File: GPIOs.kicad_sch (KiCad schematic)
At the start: 0 parts

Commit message: [feat] Add CAN transceiver SN65VHD230
Also ran ERC checks and add some exclusion ERC for the FT230XS due to
3V3OUT being an input pin rather than output pin
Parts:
- added J2: SWD, symbol Connector:Conn_01x03_Pin
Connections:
- new net SWCLK: J2.2 (Pin_2)
- new net SWDIO: J2.1 (Pin_1)
- new net TRACE_SWO: J2.3 (Pin_3)
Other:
- note added: "Serial Wire Debugger"
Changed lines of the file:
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@@
 	(generator_version "10.0")
 	(paper "A4")
+	(rectangle
+		(start 19.05 20.32)
+		(end 55.88 39.37)
+		(stroke
+			(width 0)
+			(type default)
+		)
+		(fill
+			(type none)
+		)
+	)
+	(text "Serial Wire Debugger"
+		(exclude_from_sim no)
+		(at 28.702 18.542 0)
+		(effects
+			(font
+				(size 1.27 1.27)
+			)
+		)
+	)
+	(wire
+		(pts
+			(xy 30.48 29.21) (xy 35.56 29.21)
+		)
+		(stroke
+			(width 0)
+			(type default)
+		)
+	)
+	(wire
+		(pts
+			(xy 30.48 31.75) (xy 35.56 31.75)
+		)
+		(stroke
+			(width 0)
+			(type default)
+		)
+	)
+	(wire
+		(pts
+			(xy 30.48 34.29) (xy 35.56 34.29)
+		)
+		(stroke
+			(width 0)
+			(type default)
+		)
+	)
+	(hierarchical_label "SWDIO"
+		(shape input)
+		(at 35.56 29.21 0)
+		(effects
+			(font
+				(size 1.27 1.27)
+			)
+			(justify left)
+		)
+	)
+	(hierarchical_label "TRACE_SWO"
+		(shape input)
+		(at 35.56 34.29 0)
+		(effects
+			(font
+				(size 1.27 1.27)
+			)
+			(justify left)
+		)
+	)
+	(hierarchical_label "SWCLK"
+		(shape input)
+		(at 35.56 31.75 0)
+		(effects
+			(font
+				(size 1.27 1.27)
+			)
+			(justify left)
+		)
+	)
+	(symbol
+		(lib_id "Connector:Conn_01x03_Pin")
+		(at 25.4 31.75 0)
+		(unit 1)
+		(body_style 1)
+		(exclude_from_sim no)
+		(in_bom yes)
+		(on_board yes)
+		(in_pos_files yes)
+		(dnp no)
+		(fields_autoplaced yes)
+		(property "Reference" "J2"
+			(at 26.035 24.13 0)
+			(show_name no)
+			(do_not_autoplace no)
+			(effects
+				(font
+					(size 1.27 1.27)
+				)
+			)
+		)
+		(property "Value" "SWD"
+			(at 26.035 26.67 0)
+			(show_name no)
+			(do_not_autoplace no)
+			(effects
+				(font
+					(size 1.27 1.27)
+				)
+			)
+		)
+		(property "Footprint" ""
+			(at 25.4 31.75 0)
+			(hide yes)
+			(show_name no)
+			(do_not_autoplace no)
+			(effects
+				(font
+					(size 1.27 1.27)
+				)
+			)
+		)
+		(property "Datasheet" ""
+			(at 25.4 31.75 0)
+			(hide yes)
+			(show_name no)
+			(do_not_autoplace no)
+			(effects
+				(font
+					(size 1.27 1.27)
+				)
+			)
+		)
+		(property "Description" "Generic connector, single row, 01x03, script generated"
+			(at 25.4 31.75 0)
+			(hide yes)
+			(show_name no)
+			(do_not_autoplace no)
+			(effects
+				(font
+					(size 1.27 1.27)
+				)
+			)
+		)
+		(pin "1"
+		)
+		(pin "2"
+		)
+		(pin "3"
+		)
+		(instances
+			(project "owl_v1"
+				(path "/c1d8d3e2-84ea-437a-bbb1-a2e651deb7ac/d52cdafd-bcb4-4a55-a779-8e3cd50df227"
+					(reference "J2")
+					(unit 1)
+				)
+			)
+		)
+	)
 )

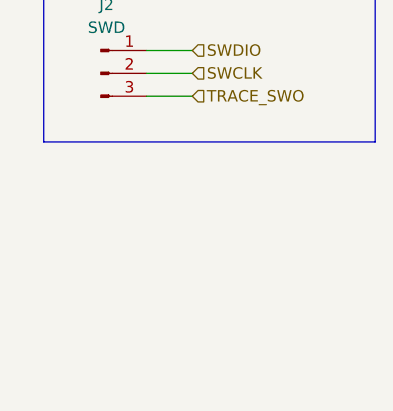
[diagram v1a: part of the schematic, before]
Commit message: [feat] Add breakout for SPI1 for IMU
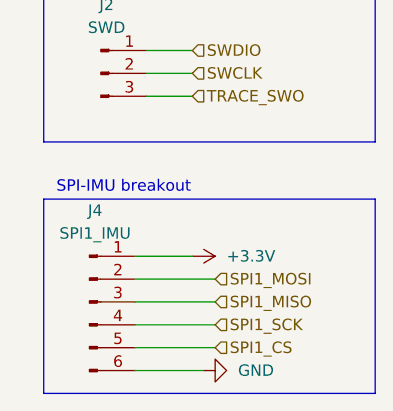
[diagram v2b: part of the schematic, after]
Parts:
- added J4: SPI1_IMU, Connector_PinHeader_2.54mm:PinHeader_1x06_P2.54mm_Vertical, symbol Connector:Conn_01x06_Pin
- J2: footprint (none) -> Connector_PinHeader_2.54mm:PinHeader_1x03_P2.54mm_Vertical; now left out of the parts list
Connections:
- new net +3.3V: J4.1 (Pin_1)
- new net GND: J4.6 (Pin_6)
- new net SPI1_CS: J4.5 (Pin_5)
- new net SPI1_MISO: J4.3 (Pin_3)
- new net SPI1_MOSI: J4.2 (Pin_2)
- new net SPI1_SCK: J4.4 (Pin_4)
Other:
- note added: "SPI-IMU breakout"

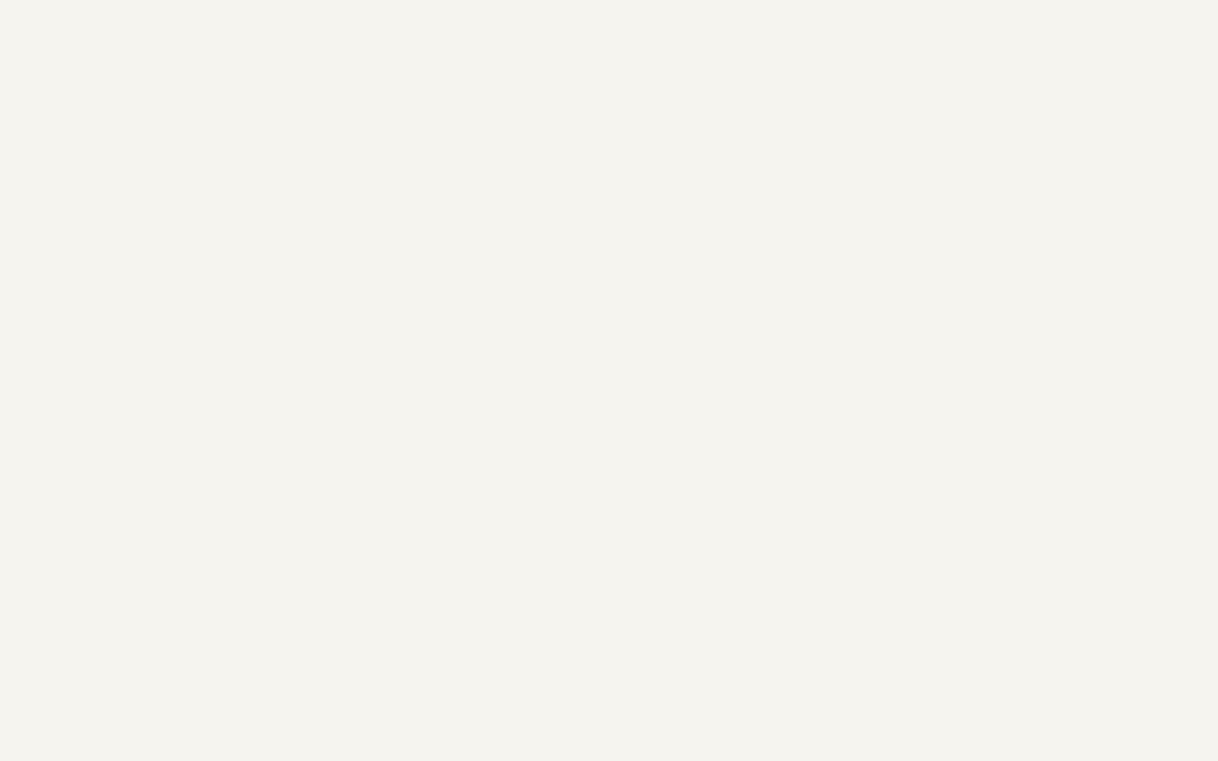
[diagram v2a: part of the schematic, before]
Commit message: [feat] Integrate MicroSD Card into the board with SPI2
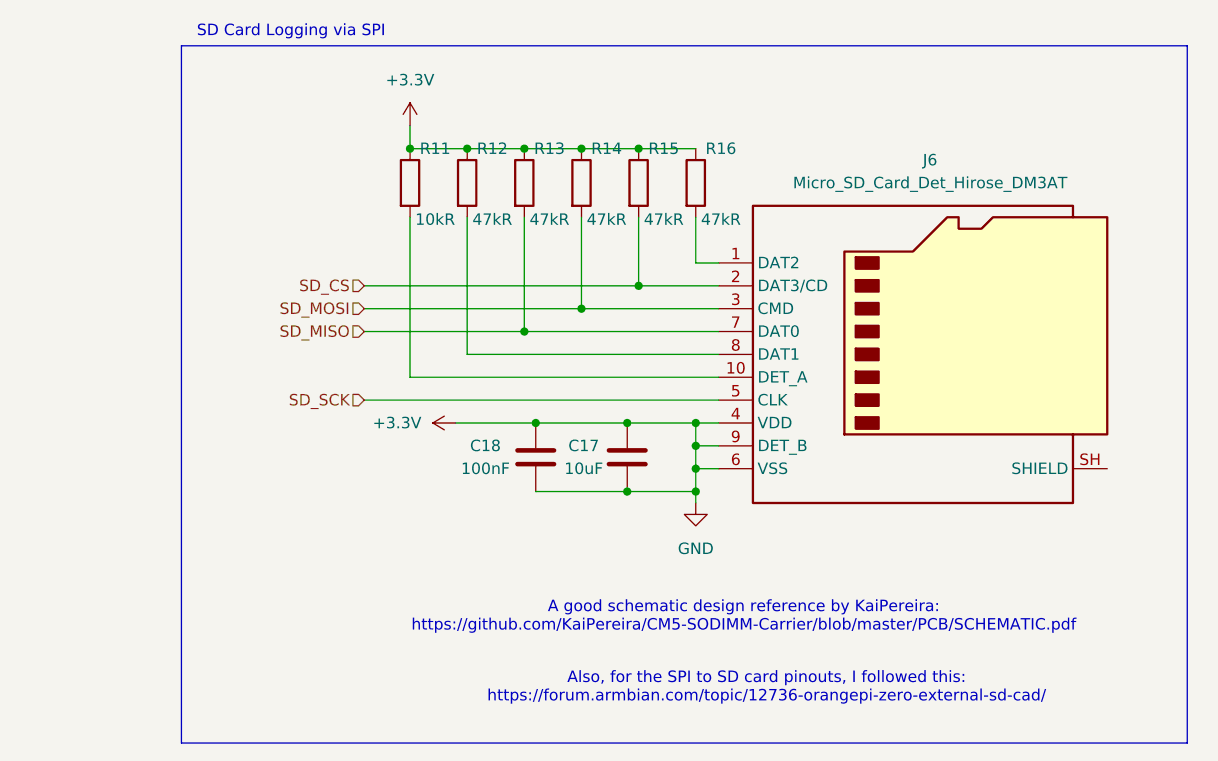
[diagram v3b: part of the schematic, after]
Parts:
- added C17: 10uF, Capacitor_SMD:C_0603_1608Metric, symbol Device:C
- added C18: 100nF, Capacitor_SMD:C_0603_1608Metric, symbol Device:C
- added J6: Micro_SD_Card_Det_Hirose_DM3AT, Connector_Card:microSD_HC_Hirose_DM3AT-SF-PEJM5, symbol Connector:Micro_SD_Card_Det_Hirose_DM3AT
- added R11: 10kR, Resistor_SMD:R_0603_1608Metric, symbol Device:R
- added R12, R13, R14, R15, R16: 47kR, Resistor_SMD:R_0603_1608Metric, symbol Device:R
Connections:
- net GND is gone; now on net +3.3V: J4.6 (Pin_6)
- net +3.3V: now also C17.1, C17.2, C18.1, C18.2, J6.4 (VDD), J6.6 (VSS), J6.9 (DET_B), R11.1, R12.1, R13.1, R14.1, R15.1, R16.1
- new net: J6.1 (DAT2), R16.2
- new net: J6.10 (DET_A), R11.2
- new net: J6.8 (DAT1), R12.2
- new net SD_CS: J6.2 (DAT3/CD), R15.2
- new net SD_MISO: J6.7 (DAT0), R13.2
- new net SD_MOSI: J6.3 (CMD), R14.2
- new net SD_SCK: J6.5 (CLK)
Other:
- note added: "A good schematic design reference by KaiPereira: https://github.com/KaiPereira/CM5-SODIMM-Carrier/blob/master/PCB/SCHEMATIC.pdf"
- note added: "Also, for the SPI to SD card pinouts, I followed this: https://forum.armbian.com/topic/12736-orangepi-zero-external-sd-cad/"
- note added: "SD Card Logging via SPI"

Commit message: [feat] Add I2C breakout
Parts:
- added J5: I2C, Connector_PinHeader_2.54mm:PinHeader_1x04_P2.54mm_Vertical, symbol Connector:Conn_01x04_Pin
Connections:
- net +3.3V: now also J5.1 (Pin_1), J5.4 (Pin_4)
- new net I2C_SCLK: J5.3 (Pin_3)
- new net I2C_SDA: J5.2 (Pin_2)
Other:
- note added: "I2C Breakout"
- note added: "I2C_CS can be used via GPIO"
- moved on the sheet: C17, C18, J6, R11, R12, R13, R14, R15, R16

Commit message: [feat] Add OLED I2C breakout for display, Add general purpose GPIOs
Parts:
- added J7: I2C OLED, Connector_PinSocket_2.54mm:PinSocket_1x04_P2.54mm_Vertical, symbol Connector:Conn_01x04_Socket
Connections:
- net +3.3V: now also J7.1 (Pin_1); no longer C17.2, C18.2, J4.6 (Pin_6), J5.4 (Pin_4), J6.6 (VSS), J6.9 (DET_B)
- new net GND: C17.2, C18.2, J4.6 (Pin_6), J5.4 (Pin_4), J6.6 (VSS), J6.9 (DET_B), J7.2 (Pin_2)
- new net OLED_SCL: J7.3 (Pin_3)
- new net OLED_SDA: J7.4 (Pin_4)
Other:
- note added: "0.96" OLED Display Module (128x64)"
- note added: "I2C Display to use"
- note added: "OLED Display Module Integration"

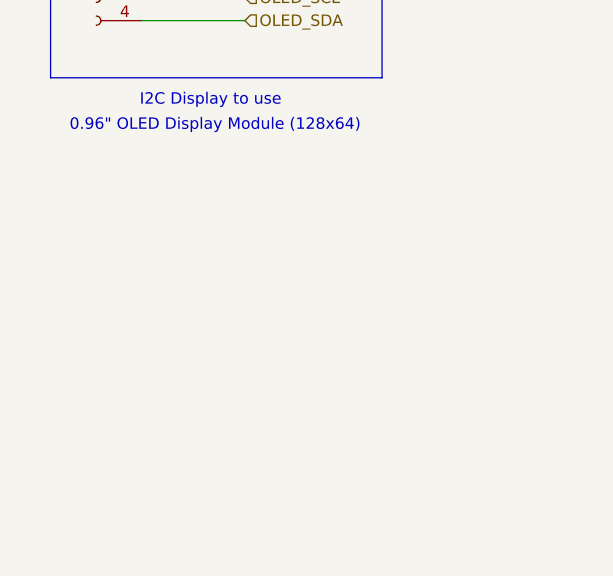
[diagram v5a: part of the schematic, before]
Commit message: [feat] Add footprints for external GPIOs
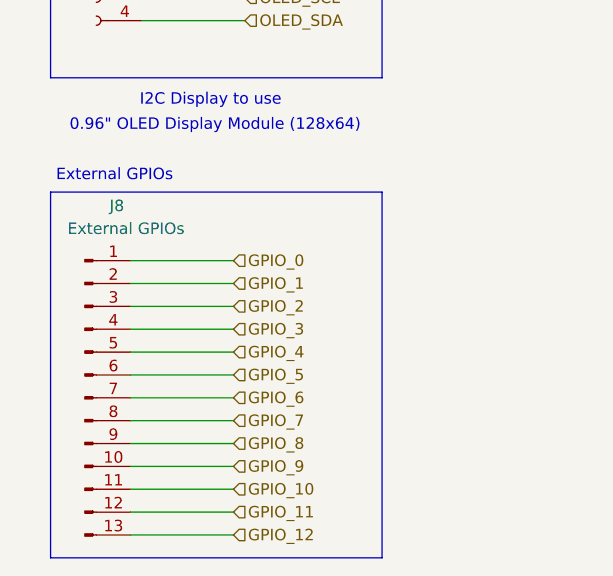
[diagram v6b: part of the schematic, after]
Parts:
- added J8: External GPIOs, Connector_PinHeader_2.54mm:PinHeader_1x13_P2.54mm_Vertical, symbol Connector:Conn_01x13_Pin
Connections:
- new net GPIO_0: J8.1 (Pin_1)
- new net GPIO_1: J8.2 (Pin_2)
- new net GPIO_10: J8.11 (Pin_11)
- new net GPIO_11: J8.12 (Pin_12)
- new net GPIO_12: J8.13 (Pin_13)
- new net GPIO_2: J8.3 (Pin_3)
- new net GPIO_3: J8.4 (Pin_4)
- new net GPIO_4: J8.5 (Pin_5)
- new net GPIO_5: J8.6 (Pin_6)
- new net GPIO_6: J8.7 (Pin_7)
- new net GPIO_7: J8.8 (Pin_8)
- new net GPIO_8: J8.9 (Pin_9)
- new net GPIO_9: J8.10 (Pin_10)
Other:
- note added: "External GPIOs"

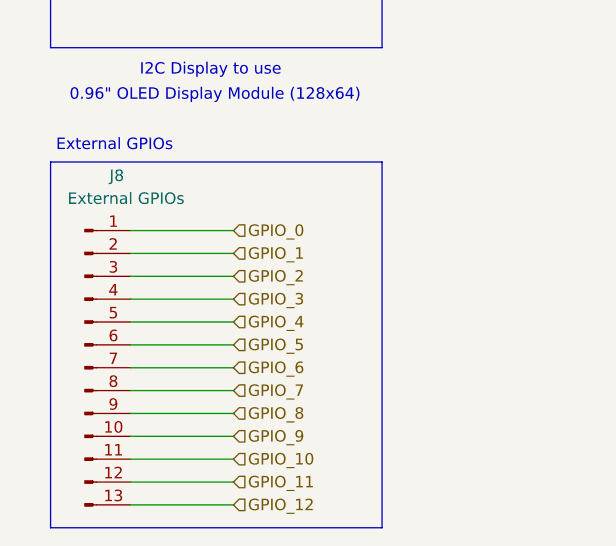
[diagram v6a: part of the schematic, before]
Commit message: [refactor] Remove GPIO12 and GPIO13 for LED green and blue
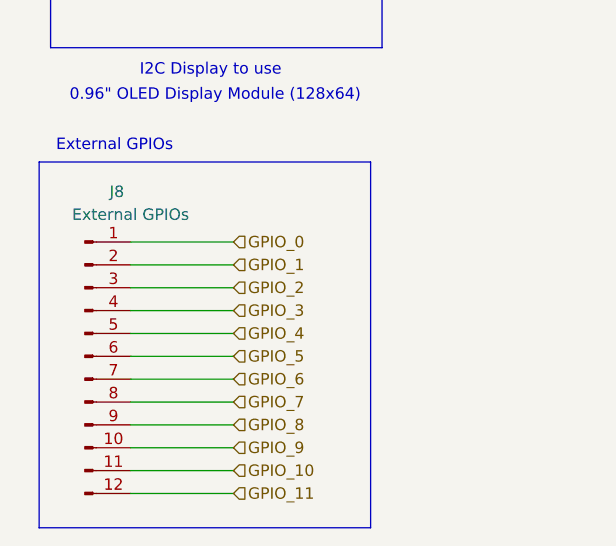
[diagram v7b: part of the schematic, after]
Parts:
- J8: symbol Connector:Conn_01x13_Pin -> Connector:Conn_01x12_Pin
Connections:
- removed net GPIO_12: J8.13 (Pin_13)
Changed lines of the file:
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@@
 	(paper "A4")
 	(rectangle
-		(start 19.05 142.24)
-		(end 55.88 182.88)
+		(start 17.78 142.24)
+		(end 54.61 182.88)
 		(stroke
 			(width 0)
@@
 	(wire
 		(pts
-			(xy 27.94 152.4) (xy 39.37 152.4)
+			(xy 27.94 171.45) (xy 39.37 171.45)
+		)
+		(stroke
+			(width 0)
+			(type default)
+		)
+	)
+	(wire
+		(pts
+			(xy 27.94 168.91) (xy 39.37 168.91)
 		)
 		(stroke
@@
 	(wire
 		(pts
-			(xy 27.94 154.94) (xy 39.37 154.94)
-		)
-		(stroke
-			(width 0)
-			(type default)
-		)
-	)
-	(wire
-		(pts
 			(xy 121.92 44.45) (xy 124.46 44.45)
 		)
@@
 	(wire
 		(pts
-			(xy 27.94 175.26) (xy 39.37 175.26)
+			(xy 27.94 153.67) (xy 39.37 153.67)
 		)
 		(stroke
@@
 	(wire
 		(pts
-			(xy 27.94 167.64) (xy 39.37 167.64)
-		)
-		(stroke
-			(width 0)
-			(type default)
-		)
-	)
-	(wire
-		(pts
-			(xy 27.94 160.02) (xy 39.37 160.02)
-		)
-		(stroke
-			(width 0)
-			(type default)
-		)
-	)
-	(wire
-		(pts
 			(xy 29.21 118.11) (xy 39.37 118.11)
 		)
@@
 	(wire
 		(pts
+			(xy 27.94 173.99) (xy 39.37 173.99)
+		)
+		(stroke
+			(width 0)
+			(type default)
+		)
+	)
+	(wire
+		(pts
 			(xy 104.14 69.85) (xy 114.3 69.85)
 		)
@@
 	(wire
 		(pts
-			(xy 27.94 157.48) (xy 39.37 157.48)
+			(xy 27.94 179.07) (xy 39.37 179.07)
 		)
 		(stroke
@@
 	(wire
 		(pts
+			(xy 27.94 163.83) (xy 39.37 163.83)
+		)
+		(stroke
+			(width 0)
+			(type default)
+		)
+	)
+	(wire
+		(pts
 			(xy 29.21 123.19) (xy 40.64 123.19)
 		)
@@
 	(wire
 		(pts
+			(xy 27.94 166.37) (xy 39.37 166.37)
+		)
+		(stroke
+			(width 0)
+			(type default)
+		)
+	)
+	(wire
+		(pts
 			(xy 124.46 67.31) (xy 121.92 67.31)
 		)
@@
 	(wire
 		(pts
+			(xy 27.94 161.29) (xy 39.37 161.29)
+		)
+		(stroke
+			(width 0)
+			(type default)
+		)
+	)
+	(wire
+		(pts
 			(xy 29.21 64.77) (xy 36.83 64.77)
 		)
@@
 	(wire
 		(pts
-			(xy 27.94 165.1) (xy 39.37 165.1)
+			(xy 27.94 158.75) (xy 39.37 158.75)
 		)
 		(stroke
@@
 	(wire
 		(pts
-			(xy 27.94 172.72) (xy 39.37 172.72)
-		)
-		(stroke
-			(width 0)
-			(type default)
-		)
-	)
-	(wire
-		(pts
 			(xy 121.92 39.37) (xy 121.92 44.45)
 		)
@@
 	(wire
 		(pts
-			(xy 27.94 162.56) (xy 39.37 162.56)
-		)
-		(stroke
-			(width 0)
-			(type default)
-		)
-	)
-	(wire
-		(pts
 			(xy 115.57 31.75) (xy 121.92 31.75)
 		)
@@
 	(wire
 		(pts
-			(xy 27.94 170.18) (xy 39.37 170.18)
-		)
-		(stroke
-			(width 0)
-			(type default)
-		)
-	)
-	(wire
-		(pts
 			(xy 85.09 49.53) (xy 109.22 49.53)
 		)
@@
 	(wire
 		(pts
-			(xy 27.94 180.34) (xy 39.37 180.34)
-		)
-		(stroke
-			(width 0)
-			(type default)
-		)
-	)
-	(wire
-		(pts
 			(xy 96.52 39.37) (xy 96.52 54.61)
 		)
@@
 	(wire
 		(pts
-			(xy 27.94 177.8) (xy 39.37 177.8)
-		)
-		(stroke
-			(width 0)
-			(type default)
-		)
-	)
-	(wire
-		(pts
 			(xy 102.87 31.75) (xy 109.22 31.75)
 		)
@@
 	(wire
 		(pts
+			(xy 27.94 156.21) (xy 39.37 156.21)
+		)
+		(stroke
+			(width 0)
+			(type default)
+		)
+	)
+	(wire
+		(pts
 			(xy 121.92 64.77) (xy 121.92 67.31)
 		)
@@
 	(wire
 		(pts
-			(xy 27.94 149.86) (xy 39.37 149.86)
+			(xy 27.94 151.13) (xy 39.37 151.13)
 		)
 		(stroke
@@
 	(wire
 		(pts
+			(xy 27.94 176.53) (xy 39.37 176.53)
+		)
+		(stroke
+			(width 0)
+			(type default)
+		)
+	)
+	(wire
+		(pts
 			(xy 109.22 39.37) (xy 109.22 49.53)
 		)
@@
 	(hierarchical_label "GPIO_6"
 		(shape input)
-		(at 39.37 165.1 0)
+		(at 39.37 166.37 0)
 		(effects
 			(font
@@
 	(hierarchical_label "GPIO_5"
 		(shape input)
-		(at 39.37 162.56 0)
+		(at 39.37 163.83 0)
 		(effects
 			(font
@@
 	(hierarchical_label "GPIO_11"
 		(shape input)
-		(at 39.37 177.8 0)
-		(effects
-			(font
-				(size 1.27 1.27)
-			)
-			(justify left)
-		)
-	)
-	(hierarchical_label "GPIO_12"
-		(shape input)
-		(at 39.37 180.34 0)
+		(at 39.37 179.07 0)
 		(effects
 			(font
@@
 	(hierarchical_label "GPIO_7"
 		(shape input)
-		(at 39.37 167.64 0)
+		(at 39.37 168.91 0)
 		(effects
 			(font
@@
 	(hierarchical_label "GPIO_1"
 		(shape input)
-		(at 39.37 152.4 0)
+		(at 39.37 153.67 0)
 		(effects
 			(font
@@
 	(hierarchical_label "GPIO_8"
 		(shape input)
-		(at 39.37 170.18 0)
+		(at 39.37 171.45 0)
 		(effects
 			(font
@@
 	(hierarchical_label "GPIO_9"
 		(shape input)
-		(at 39.37 172.72 0)
+		(at 39.37 173.99 0)
 		(effects
 			(font
@@
 	(hierarchical_label "GPIO_10"
 		(shape input)
-		(at 39.37 175.26 0)
+		(at 39.37 176.53 0)
 		(effects
 			(font
@@
 	(hierarchical_label "GPIO_4"
 		(shape input)
-		(at 39.37 160.02 0)
+		(at 39.37 161.29 0)
 		(effects
 			(font
@@
 	(hierarchical_label "GPIO_3"
 		(shape input)
-		(at 39.37 157.48 0)
+		(at 39.37 158.75 0)
 		(effects
 			(font
@@
 	(hierarchical_label "GPIO_2"
 		(shape input)
-		(at 39.37 154.94 0)
+		(at 39.37 156.21 0)
 		(effects
 			(font
@@
 	(hierarchical_label "GPIO_0"
 		(shape input)
-		(at 39.37 149.86 0)
+		(at 39.37 151.13 0)
 		(effects
 			(font
@@
 	)
 	(symbol
-		(lib_id "Connector:Conn_01x13_Pin")
-		(at 22.86 165.1 0)
+		(lib_id "Connector:Conn_01x12_Pin")
+		(at 22.86 163.83 0)
 		(unit 1)
 		(body_style 1)
@@
 		(dnp no)
 		(property "Reference" "J8"
-			(at 26.416 143.764 0)
+			(at 26.416 145.542 0)
 			(show_name no)
 			(do_not_autoplace no)
@@
 		)
 		(property "Value" "External GPIOs"
-			(at 27.432 146.304 0)
+			(at 27.94 148.082 0)
 			(show_name no)
 			(do_not_autoplace no)
@@
 		)
 		(property "Footprint" "Connector_PinHeader_2.54mm:PinHeader_1x13_P2.54mm_Vertical"
-			(at 22.86 165.1 0)
+			(at 22.86 163.83 0)
 			(hide yes)
 			(show_name no)
@@
 		)
 		(property "Datasheet" ""
-			(at 22.86 165.1 0)
+			(at 22.86 163.83 0)
 			(hide yes)
 			(show_name no)
@@
 			)
 		)
-		(property "Description" "Generic connector, single row, 01x13, script generated"
-			(at 22.86 165.1 0)
+		(property "Description" "Generic connector, single row, 01x12, script generated"
+			(at 22.86 163.83 0)
 			(hide yes)
 			(show_name no)
@@
 		(pin "11"
 		)
-		(pin "13"
-		)
 		(pin "4"

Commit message: [feat] Integrate external battery
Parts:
- J8: footprint Connector_PinHeader_2.54mm:PinHeader_1x13_P2.54mm_Vertical -> Connector_PinHeader_2.54mm:PinHeader_1x12_P2.54mm_Vertical
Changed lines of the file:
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@@
 			)
 		)
-		(property "Footprint" "Connector_PinHeader_2.54mm:PinHeader_1x13_P2.54mm_Vertical"
+		(property "Footprint" "Connector_PinHeader_2.54mm:PinHeader_1x12_P2.54mm_Vertical"
 			(at 22.86 163.83 0)
 			(hide yes)
